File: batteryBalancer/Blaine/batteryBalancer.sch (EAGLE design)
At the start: 34 parts

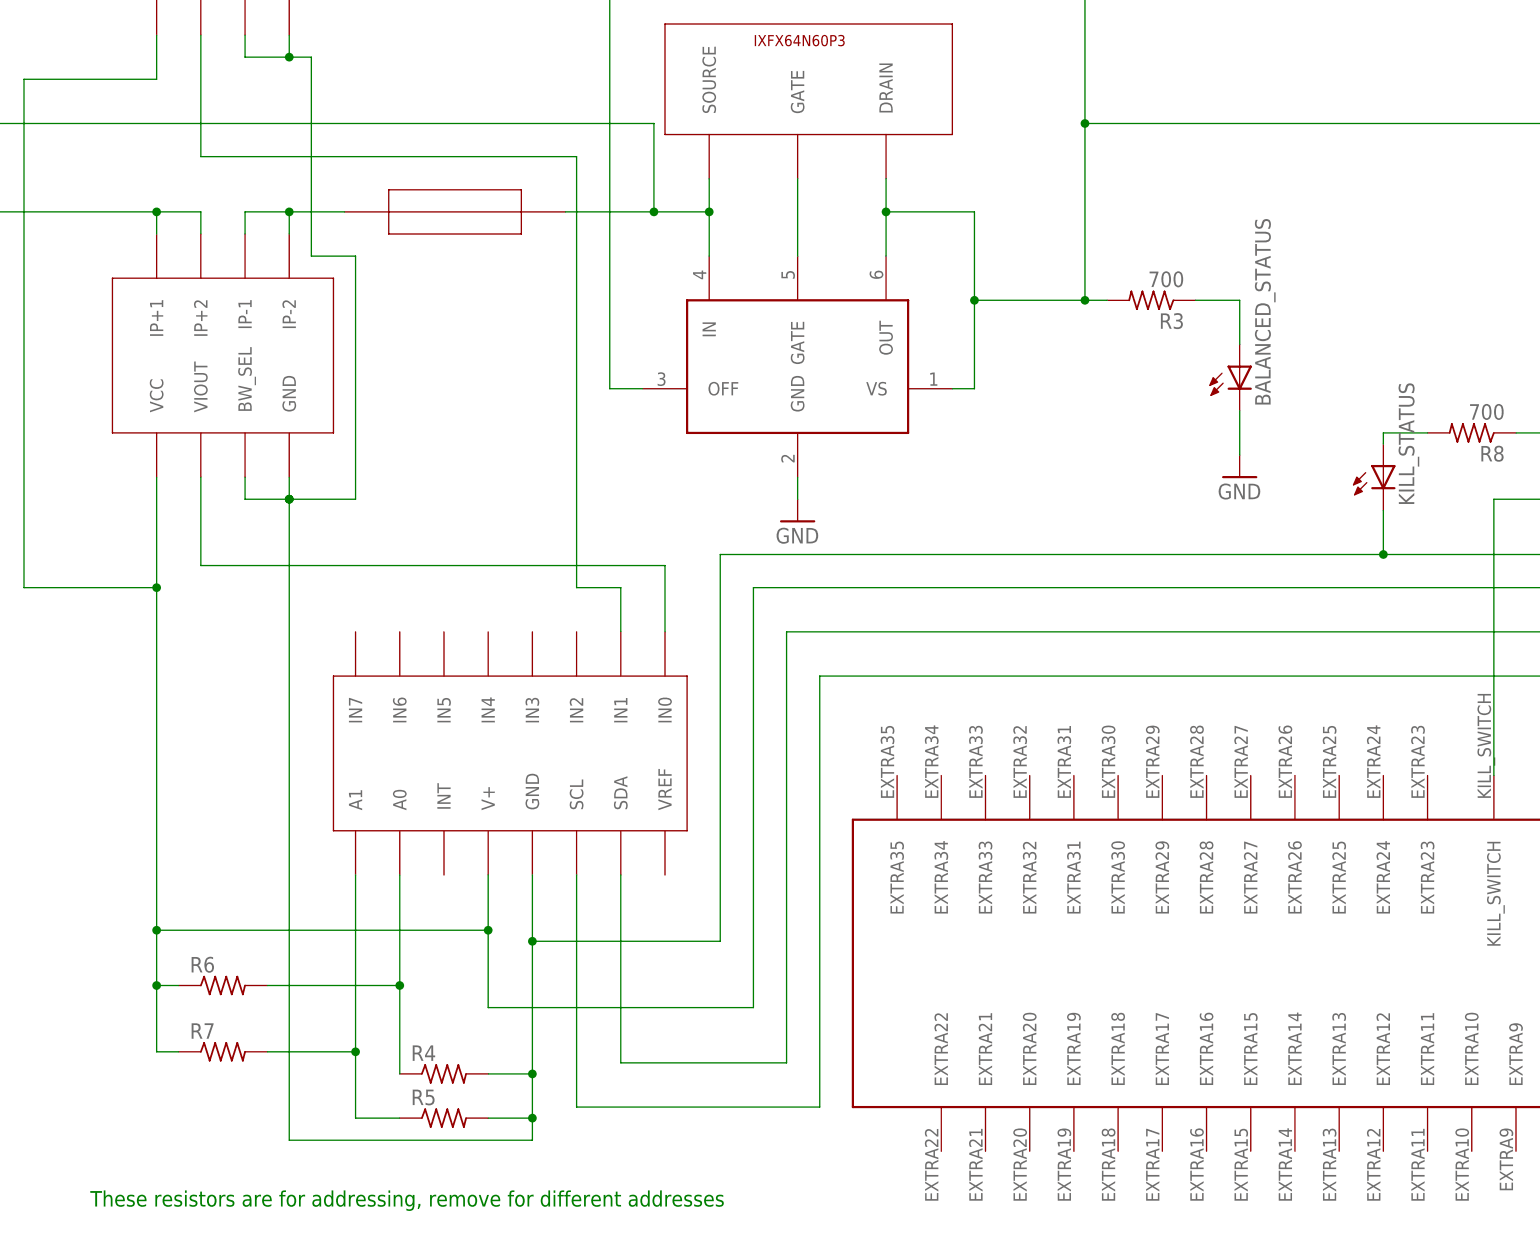
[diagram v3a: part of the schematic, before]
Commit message: Applied changes suggested in design review
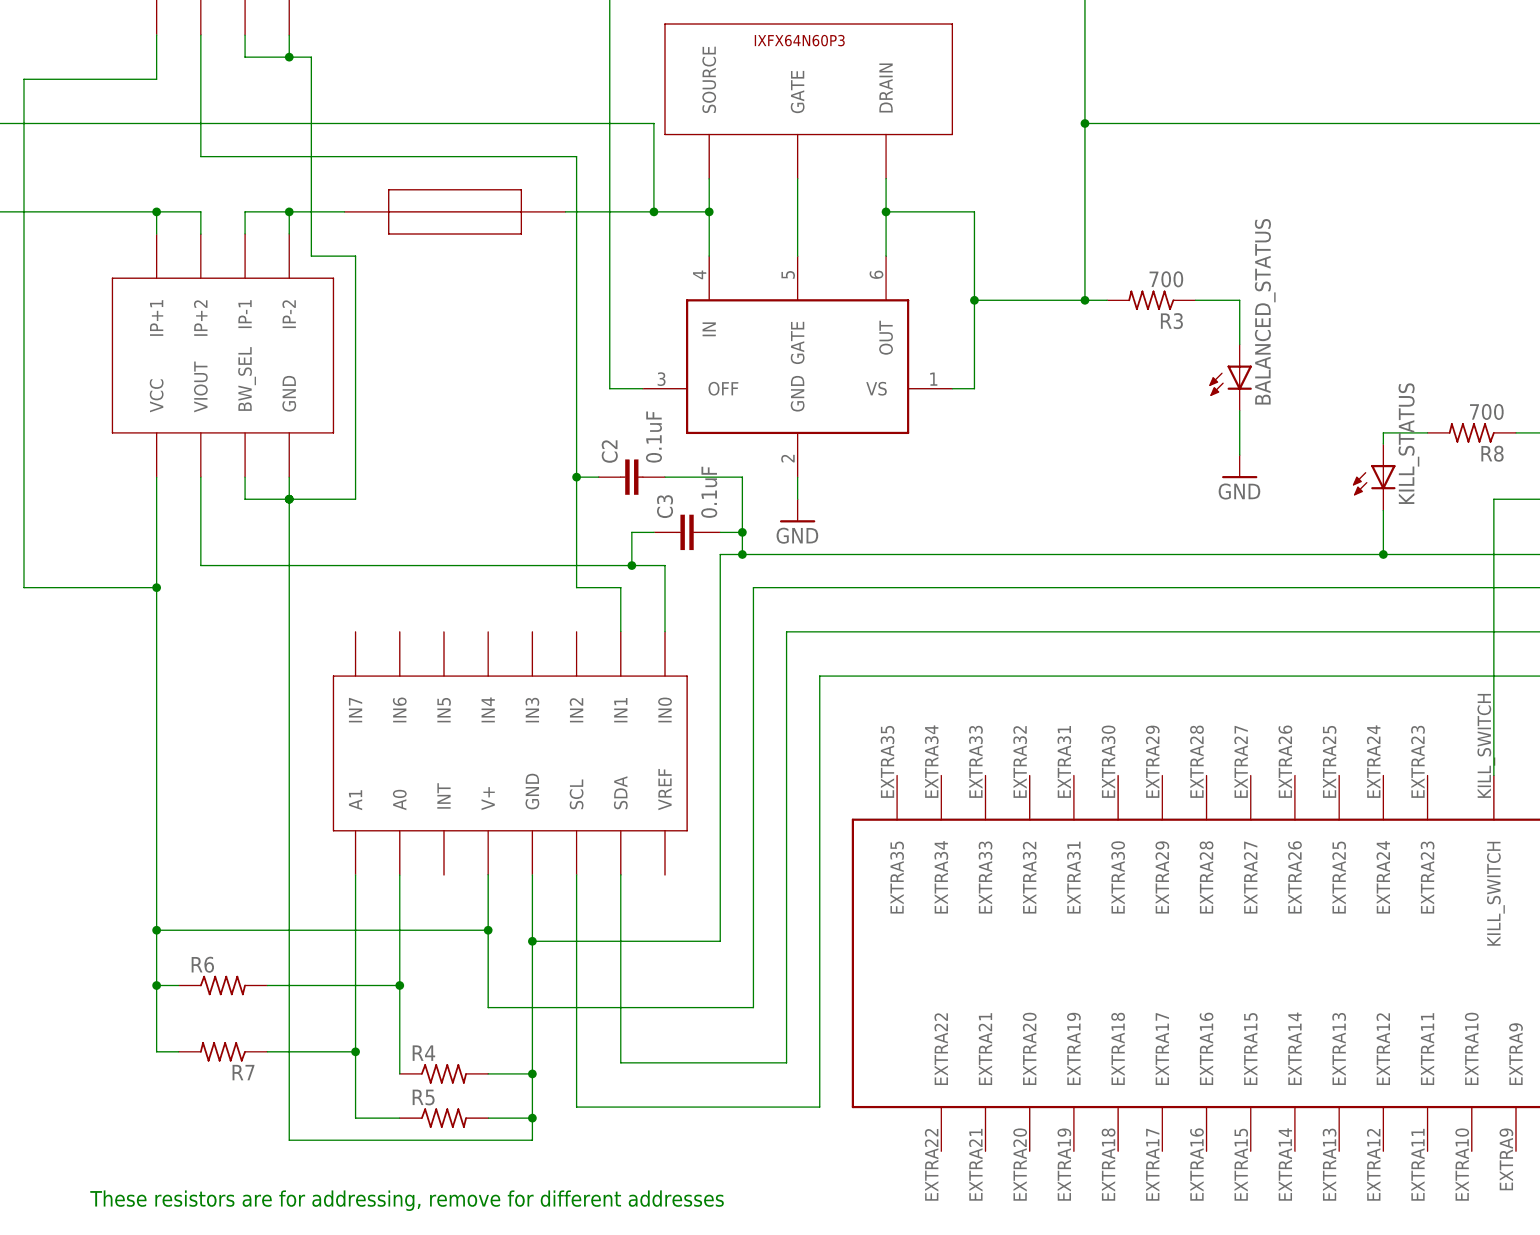
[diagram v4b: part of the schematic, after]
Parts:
- added C2, C3: 0.1uF, SparkFun-Capacitors:0.1UF-KIT-EZ-50V-20%
- R4, R5, R6, R7: device rcl:R-US_MELF0204W -> resistor:R-US_0204/5
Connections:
- net N$1 renamed PORT_SOURCE
- net 3.3V: now also R7.2; no longer R7.1
- net ADC_A1: now also R7.1; no longer R7.2
- net LOGIC_GND: now also C2.2, C3.2
- net PORT_CURRENT: now also C3.1
- net STBD_CURRENT: now also C2.1
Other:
- moved on the sheet: R7
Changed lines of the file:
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@@
 <?xml version="1.0" encoding="utf-8"?>
 <!DOCTYPE eagle SYSTEM "eagle.dtd">
-<eagle version="8.3.2">
+<eagle version="8.4.0">
 <drawing>
 <settings>
@@
 <part name="PORT_FUSE" library="01220083Z" deviceset="01220083Z" device=""/>
 <part name="ADC" library="ADC128D818" deviceset="ADC128D818" device=""/>
-<part name="R4" library="rcl" library_urn="urn:adsk.eagle:library:334" deviceset="R-US_" device="MELF0204W" package3d_urn="urn:adsk.eagle:package:23584/1"/>
-<part name="R5" library="rcl" library_urn="urn:adsk.eagle:library:334" deviceset="R-US_" device="MELF0204W" package3d_urn="urn:adsk.eagle:package:23584/1"/>
-<part name="R6" library="rcl" library_urn="urn:adsk.eagle:library:334" deviceset="R-US_" device="MELF0204W" package3d_urn="urn:adsk.eagle:package:23584/1"/>
-<part name="R7" library="rcl" library_urn="urn:adsk.eagle:library:334" deviceset="R-US_" device="MELF0204W" package3d_urn="urn:adsk.eagle:package:23584/1"/>
+<part name="R4" library="resistor" library_urn="urn:adsk.eagle:library:348" deviceset="R-US_" device="0204/5" package3d_urn="urn:adsk.eagle:package:25955/1"/>
+<part name="R5" library="resistor" library_urn="urn:adsk.eagle:library:348" deviceset="R-US_" device="0204/5" package3d_urn="urn:adsk.eagle:package:25955/1"/>
+<part name="R6" library="resistor" library_urn="urn:adsk.eagle:library:348" deviceset="R-US_" device="0204/5" package3d_urn="urn:adsk.eagle:package:25955/1"/>
+<part name="R7" library="resistor" library_urn="urn:adsk.eagle:library:348" deviceset="R-US_" device="0204/5" package3d_urn="urn:adsk.eagle:package:25955/1"/>
 <part name="STBD_CS" library="ACS722" deviceset="ACS722" device=""/>
 <part name="PORT_CS" library="ACS722" deviceset="ACS722" device=""/>
@@
 <part name="R8" library="rcl" library_urn="urn:adsk.eagle:library:334" deviceset="R-US_" device="0207/7" package3d_urn="urn:adsk.eagle:package:23493/1" value="700"/>
 <part name="KILL_STATUS" library="LTST-S270GKT" deviceset="LTST-S270GKT" device=""/>
+<part name="C2" library="SparkFun-Capacitors" deviceset="0.1UF" device="-KIT-EZ-50V-20%" value="0.1uF"/>
+<part name="C3" library="SparkFun-Capacitors" deviceset="0.1UF" device="-KIT-EZ-50V-20%" value="0.1uF"/>
 </parts>
 <sheets>
@@
 <instance part="R5" gate="G$1" x="147.32" y="50.8"/>
 <instance part="R6" gate="G$1" x="121.92" y="66.04"/>
-<instance part="R7" gate="G$1" x="121.92" y="58.42"/>
+<instance part="R7" gate="G$1" x="121.92" y="58.42" rot="R180"/>
 <instance part="STBD_CS" gate="G$1" x="124.46" y="187.96"/>
 <instance part="PORT_CS" gate="G$1" x="124.46" y="137.16"/>
@@
 <instance part="R8" gate="G$1" x="265.43" y="129.54" rot="R180"/>
 <instance part="KILL_STATUS" gate="G$1" x="255.27" y="125.73"/>
+<instance part="C2" gate="G$1" x="170.18" y="124.46" rot="R90"/>
+<instance part="C3" gate="G$1" x="176.53" y="118.11" rot="R90"/>
 </instances>
 <busses>
@@
 <wire x1="326.39" y1="90.17" x2="326.39" y2="100.33" width="0.1524" layer="91"/>
 <junction x="326.39" y="100.33"/>
-<wire x1="179.07" y1="115.57" x2="255.27" y2="115.57" width="0.1524" layer="91"/>
+<wire x1="179.07" y1="115.57" x2="181.61" y2="115.57" width="0.1524" layer="91"/>
+<wire x1="181.61" y1="115.57" x2="255.27" y2="115.57" width="0.1524" layer="91"/>
 <wire x1="255.27" y1="115.57" x2="287.02" y2="115.57" width="0.1524" layer="91"/>
 <wire x1="287.02" y1="115.57" x2="326.39" y2="115.57" width="0.1524" layer="91"/>
@@
 <wire x1="358.14" y1="114.3" x2="326.39" y2="114.3" width="0.1524" layer="91"/>
 <junction x="326.39" y="114.3"/>
+<pinref part="C3" gate="G$1" pin="2"/>
+<wire x1="179.07" y1="118.11" x2="181.61" y2="118.11" width="0.1524" layer="91"/>
+<wire x1="181.61" y1="118.11" x2="181.61" y2="115.57" width="0.1524" layer="91"/>
+<junction x="181.61" y="115.57"/>
+<pinref part="C2" gate="G$1" pin="2"/>
+<wire x1="172.72" y1="124.46" x2="181.61" y2="124.46" width="0.1524" layer="91"/>
+<wire x1="181.61" y1="124.46" x2="181.61" y2="118.11" width="0.1524" layer="91"/>
+<junction x="181.61" y="118.11"/>
 </segment>
 </net>
@@
 <wire x1="114.3" y1="66.04" x2="116.84" y2="66.04" width="0.1524" layer="91"/>
 <junction x="114.3" y="66.04"/>
-<pinref part="R7" gate="G$1" pin="1"/>
-<wire x1="116.84" y1="58.42" x2="114.3" y2="58.42" width="0.1524" layer="91"/>
 <wire x1="114.3" y1="58.42" x2="114.3" y2="66.04" width="0.1524" layer="91"/>
 <pinref part="PORT_CS" gate="G$1" pin="VCC"/>
@@
 <wire x1="354.33" y1="97.79" x2="346.71" y2="97.79" width="0.1524" layer="91"/>
 <junction x="346.71" y="97.79"/>
+<pinref part="R7" gate="G$1" pin="2"/>
+<wire x1="114.3" y1="58.42" x2="116.84" y2="58.42" width="0.1524" layer="91"/>
 </segment>
 </net>
@@
 <segment>
 <pinref part="ADC" gate="G$1" pin="A1"/>
+<wire x1="137.16" y1="50.8" x2="137.16" y2="58.42" width="0.1524" layer="91"/>
+<pinref part="R5" gate="G$1" pin="1"/>
 <wire x1="137.16" y1="58.42" x2="137.16" y2="78.74" width="0.1524" layer="91"/>
-<pinref part="R7" gate="G$1" pin="2"/>
+<wire x1="137.16" y1="50.8" x2="142.24" y2="50.8" width="0.1524" layer="91"/>
+<pinref part="R7" gate="G$1" pin="1"/>
 <wire x1="127" y1="58.42" x2="137.16" y2="58.42" width="0.1524" layer="91"/>
 <junction x="137.16" y="58.42"/>
-<wire x1="137.16" y1="58.42" x2="137.16" y2="50.8" width="0.1524" layer="91"/>
-<pinref part="R5" gate="G$1" pin="1"/>
-<wire x1="137.16" y1="50.8" x2="142.24" y2="50.8" width="0.1524" layer="91"/>
 </segment>
 </net>
@@
 <wire x1="119.38" y1="124.46" x2="119.38" y2="114.3" width="0.1524" layer="91"/>
 <pinref part="ADC" gate="G$1" pin="IN0"/>
-<wire x1="119.38" y1="114.3" x2="172.72" y2="114.3" width="0.1524" layer="91"/>
+<wire x1="119.38" y1="114.3" x2="168.91" y2="114.3" width="0.1524" layer="91"/>
+<wire x1="168.91" y1="114.3" x2="172.72" y2="114.3" width="0.1524" layer="91"/>
 <wire x1="172.72" y1="114.3" x2="172.72" y2="106.68" width="0.1524" layer="91"/>
+<pinref part="C3" gate="G$1" pin="1"/>
+<wire x1="171.45" y1="118.11" x2="168.91" y2="118.11" width="0.1524" layer="91"/>
+<wire x1="168.91" y1="118.11" x2="168.91" y2="114.3" width="0.1524" layer="91"/>
+<junction x="168.91" y="114.3"/>
 </segment>
 </net>
@@
 <wire x1="119.38" y1="175.26" x2="119.38" y2="161.29" width="0.1524" layer="91"/>
 <wire x1="119.38" y1="161.29" x2="162.56" y2="161.29" width="0.1524" layer="91"/>
-<wire x1="162.56" y1="161.29" x2="162.56" y2="111.76" width="0.1524" layer="91"/>
+<wire x1="162.56" y1="161.29" x2="162.56" y2="124.46" width="0.1524" layer="91"/>
 <pinref part="ADC" gate="G$1" pin="IN1"/>
+<wire x1="162.56" y1="124.46" x2="162.56" y2="111.76" width="0.1524" layer="91"/>
 <wire x1="162.56" y1="111.76" x2="167.64" y2="111.76" width="0.1524" layer="91"/>
 <wire x1="167.64" y1="111.76" x2="167.64" y2="106.68" width="0.1524" layer="91"/>
+<pinref part="C2" gate="G$1" pin="1"/>
+<wire x1="165.1" y1="124.46" x2="162.56" y2="124.46" width="0.1524" layer="91"/>
+<junction x="162.56" y="124.46"/>
 </segment>
 </net>
@@
 </segment>
 </net>
-<net name="N$1" class="0">
+<net name="PORT_SOURCE" class="0">
 <segment>
 <pinref part="PORT_FC" gate="G$1" pin="IN"/>
